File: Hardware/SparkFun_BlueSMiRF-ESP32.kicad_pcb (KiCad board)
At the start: 2 copper layers, 41.9 x 15.2 mm, 44 parts, among them J2 Conn_01x06, Q1 Q_NMOS_DGS, Q2 Q_NMOS_DGS, SW1 Switch, U1 ESP32_Pico_Mini, U2 AP2112K-3.3

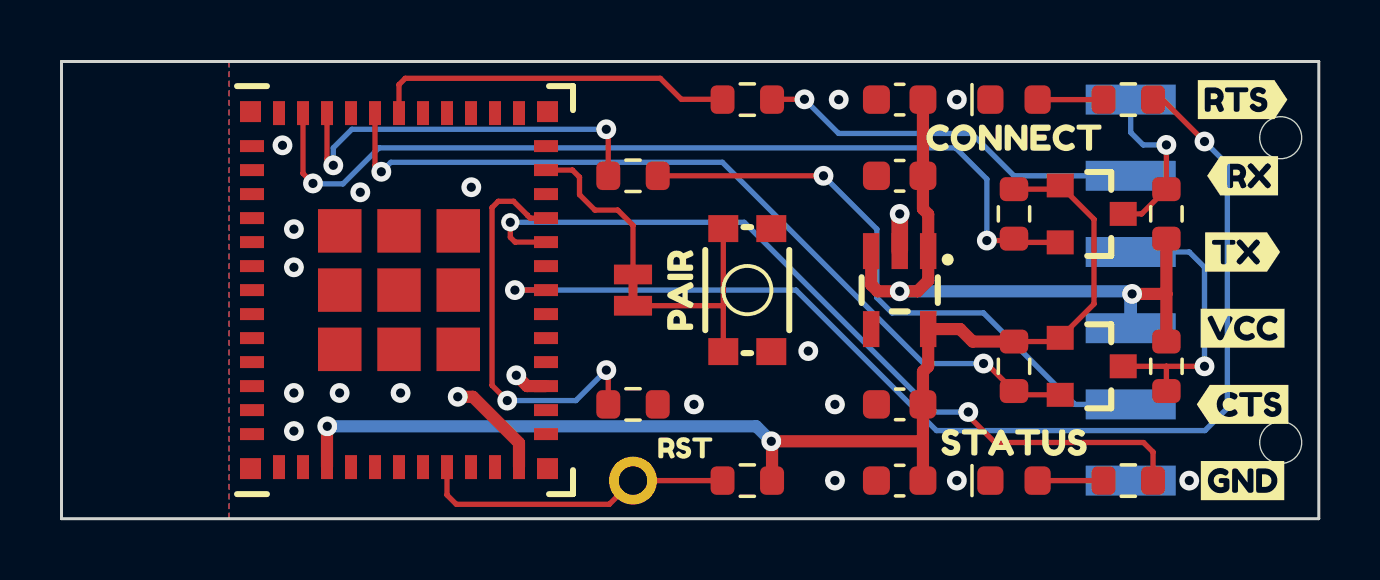
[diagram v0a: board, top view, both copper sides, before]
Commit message: Update panel with PROD_IDs.
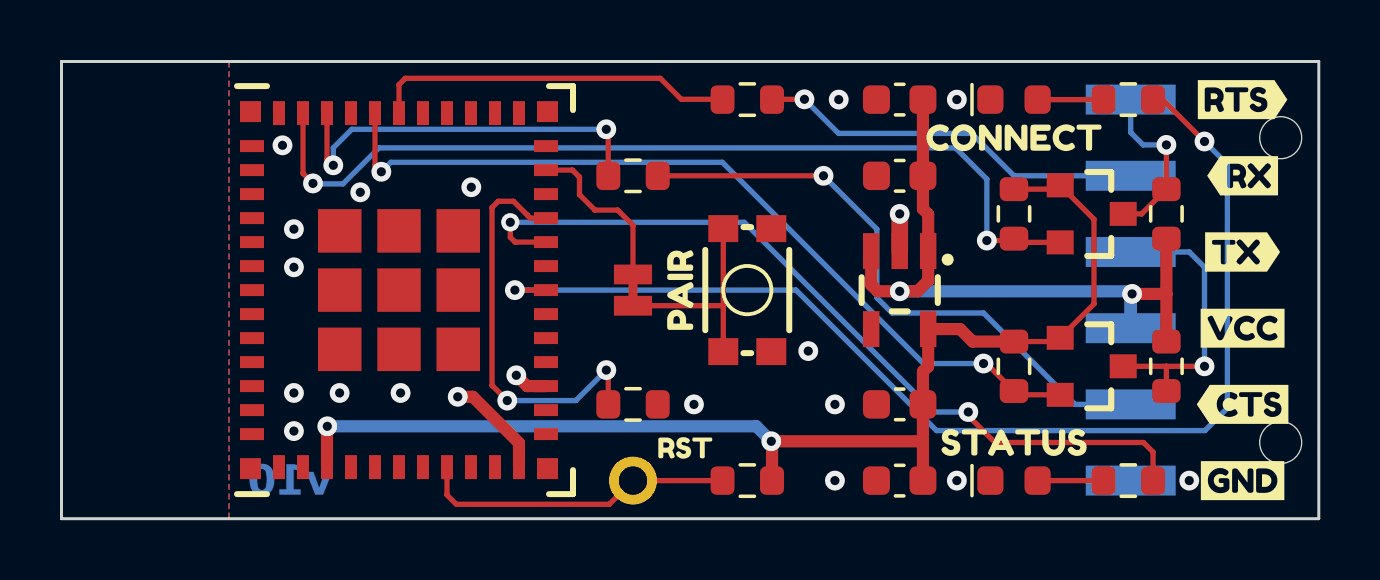
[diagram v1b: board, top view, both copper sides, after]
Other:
- board text added: "N. Seidle"
- board text added: "v10"
